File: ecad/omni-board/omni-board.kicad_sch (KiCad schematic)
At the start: 5 parts, among them J1 Motor_BTS7960_01, J2 Motor_BTS7960_02, J3 Motor_BTS7960_03, J4 Motor_BTS7960_04, U2 ESP32-S3-DevKitC

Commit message: update for production
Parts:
- removed U2: ESP32-S3-DevKitC, PCM_Espressif:ESP32-S3-DevKitC, symbol PCM_Espressif:ESP32-S3-DevKitC
- added C1: 0.1uF, Capacitor_SMD:C_1206_3216Metric_Pad1.33x1.80mm_HandSolder, symbol Device:C_Small
- added C2: 1uF, Capacitor_SMD:CP_Elec_5x5.4, symbol Device:C_Polarized_Small
- added C3: 22uF, Capacitor_SMD:CP_Elec_5x5.4, symbol Device:C_Polarized_Small
- added D1: SS14, Diode_SMD:D_SMA_Handsoldering, symbol Diode:SS14
- added D2, D3, D4: LED_Small, LED_SMD:LED_1206_3216Metric_Pad1.42x1.75mm_HandSolder, symbol Device:LED_Small
- added H1, H2, H3, H4: MountingHole_Pad, MountingHole:MountingHole_3.2mm_M3_Pad_Via, symbol Mechanical:MountingHole_Pad
- added J18, J19: Conn_01x04, Connector_Molex:Molex_KK-254_AE-6410-04A_1x04_P2.54mm_Vertical, symbol Connector_Generic:Conn_01x04
- added J7: Con Batt, Connector_AMASS:AMASS_XT60-M_1x02_P7.20mm_Vertical, symbol Connector_Generic:Conn_01x02
- added JP1: SolderJumper_3_Open, Jumper:SolderJumper-3_P2.0mm_Open_TrianglePad1.0x1.5mm, symbol Jumper:SolderJumper_3_Open
- added R1, R18, R19: 10k, Resistor_SMD:R_1206_3216Metric_Pad1.30x1.75mm_HandSolder, symbol Device:R_Small
- added R2, R21, R22: 1k, Resistor_SMD:R_1206_3216Metric_Pad1.30x1.75mm_HandSolder, symbol Device:R_Small
- added U1: ESP32-S3-Zero, omni-footprints:ESP32-S3-Zero_THT, symbol omni-symbols:ESP32-S3-Zero
- added U2: R-78E5.0-1.0, Converter_DCDC:Converter_DCDC_RECOM_R-78E-0.5_THT, symbol Converter_DCDC:R-78E5.0-1.0
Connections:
- net +3.3V: now also J18.3 (Pin_3), J19.3 (Pin_3), JP1.1 (A), R18.2, R19.2, R21.1, U1.3 (3V3)
- net EN_MOTORS: now also R1.1, U1.10 (GP7)
- net GND: now also C1.2, C2.2, C3.2, D2.1 (K), D3.1 (K), D4.1 (K), H1.1, H2.1, H3.1, H4.1, J18.4 (Pin_4), J19.4 (Pin_4), J7.1 (Pin_1), R1.2, U1.2 (GND), U2.2 (GND)
- net L_PWM_01: now also U1.5 (GP2)
- net L_PWM_02: now also U1.8 (GP5)
- net L_PWM_03: now also U1.15 (GP12)
- net L_PWM_04: now also U1.13 (GP10)
- net R_PWM_01: now also U1.4 (GP1)
- net R_PWM_02: now also U1.7 (GP4)
- net R_PWM_03: now also U1.9 (GP6)
- net R_PWM_04: now also U1.14 (GP11)
- net SBUS: now also U1.17 (GP44/RX0)
- net SCL: now also J18.1 (Pin_1), J19.1 (Pin_1), R19.1, U1.12 (GP9)
- net SDA: now also J18.2 (Pin_2), J19.2 (Pin_2), R18.1, U1.11 (GP8)
- net VCC: now also JP1.2 (C)
- new net: D2.2 (A), R21.2
- new net: C1.1, C2.1, D1.1 (K), U1.1 (5V)
- new net: D4.2 (A), R22.2
- new net: D3.2 (A), R2.2
- new net +12V: C3.1, J7.2 (Pin_2), R2.1, U2.1 (IN)
- new net +5V: D1.2 (A), JP1.3 (B), R22.1, U2.3 (OUT)
- no-connect marks 8 -> 1
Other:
- note added: "Alimentation"
- note added: "Driver BTS7960"
- note added: "ESP32S3-zero"
- note added: "Fixations"
- note added: "I2C"
- moved on the sheet: J1, J2, J3, J4

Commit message: sbus connector added
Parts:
- added J5: Conn_01x03, Connector_PinHeader_2.54mm:PinHeader_1x03_P2.54mm_Vertical, symbol Connector_Generic:Conn_01x03
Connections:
- net +5V: now also J5.2 (Pin_2)
- net GND: now also J5.3 (Pin_3)
- net SBUS: now also J5.1 (Pin_1)
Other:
- note added: "Sbus"
- moved on the sheet: J18, J19, R18, R19

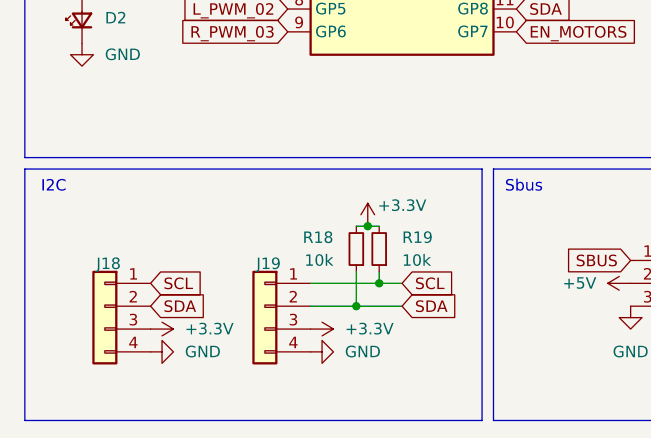
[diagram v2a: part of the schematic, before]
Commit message: add I2C connector
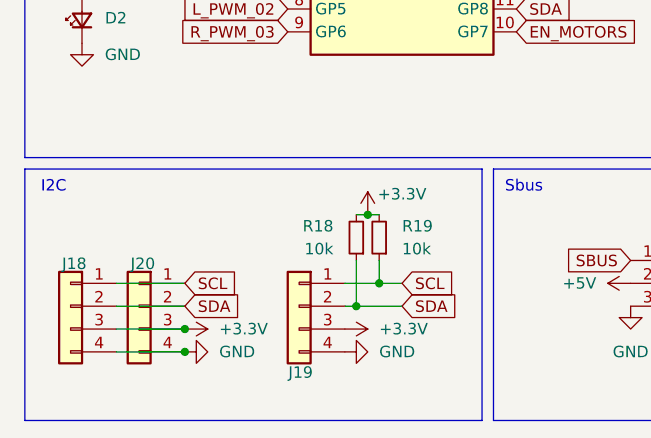
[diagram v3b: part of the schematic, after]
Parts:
- added J20: Conn_01x04, Connector_Molex:Molex_KK-254_AE-6410-04A_1x04_P2.54mm_Vertical, symbol Connector_Generic:Conn_01x04
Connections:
- net +3.3V: now also J20.3 (Pin_3)
- net GND: now also J20.4 (Pin_4)
- net SCL: now also J20.1 (Pin_1)
- net SDA: now also J20.2 (Pin_2)
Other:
- moved on the sheet: J18, J19, R18, R19
